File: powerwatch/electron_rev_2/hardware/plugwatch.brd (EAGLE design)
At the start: 57.1 x 93 mm, 87 parts, among them J1 TC2030-JLINK-NL, J2 DM3AT-SF-PEJM5, SW1 SIP3240X, SW2 SIP3240X, SW3 SIP3240X, SW4 SIP3240X, SW7 SIP3240X, U1 MAX-M8, U3 ISL29035, U37 MPU-9250, U4 NRF51822QF, U5 SAFFB1G56KB0F0A, U6 BGA725L6-ALT, U7 OPA322AIDBVT, U8 MAX740XESA, X3 16MHz, X4 ABS05-32.768KHZ-9-T

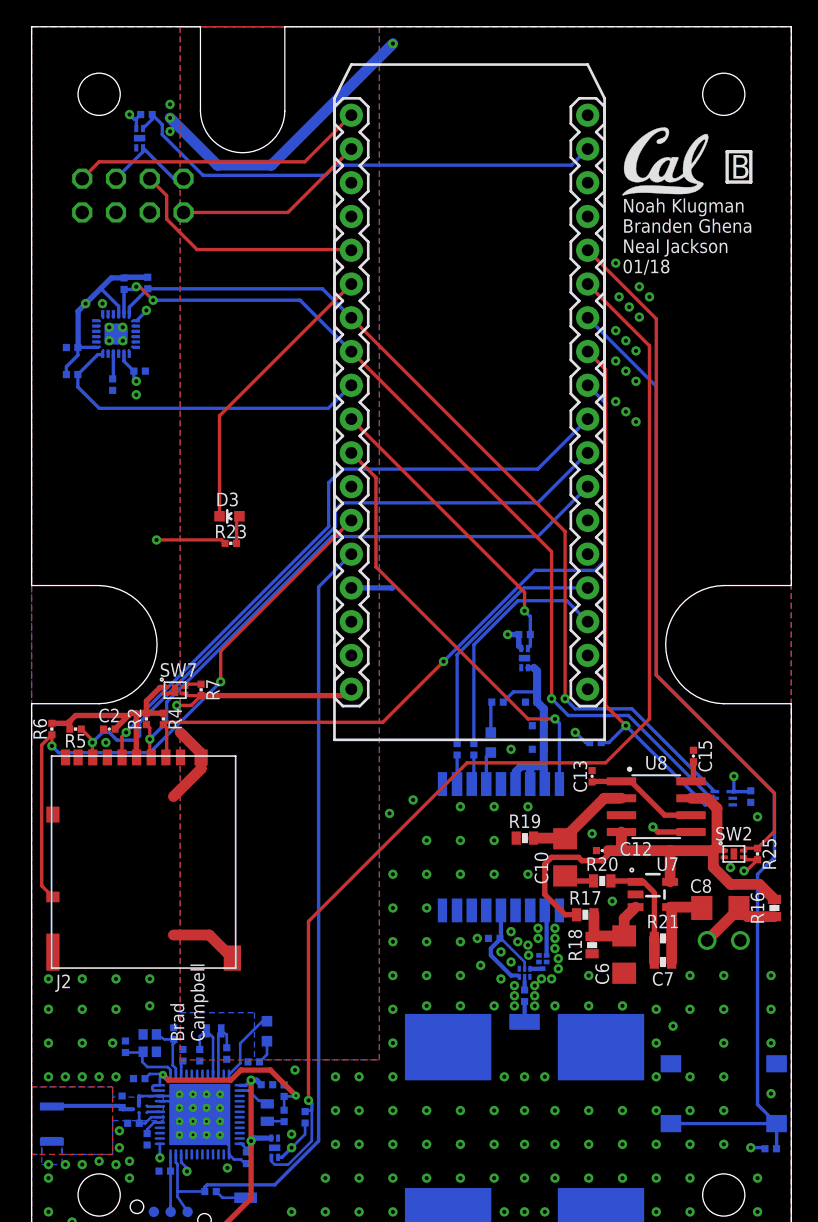
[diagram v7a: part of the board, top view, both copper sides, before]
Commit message: Add testpoints
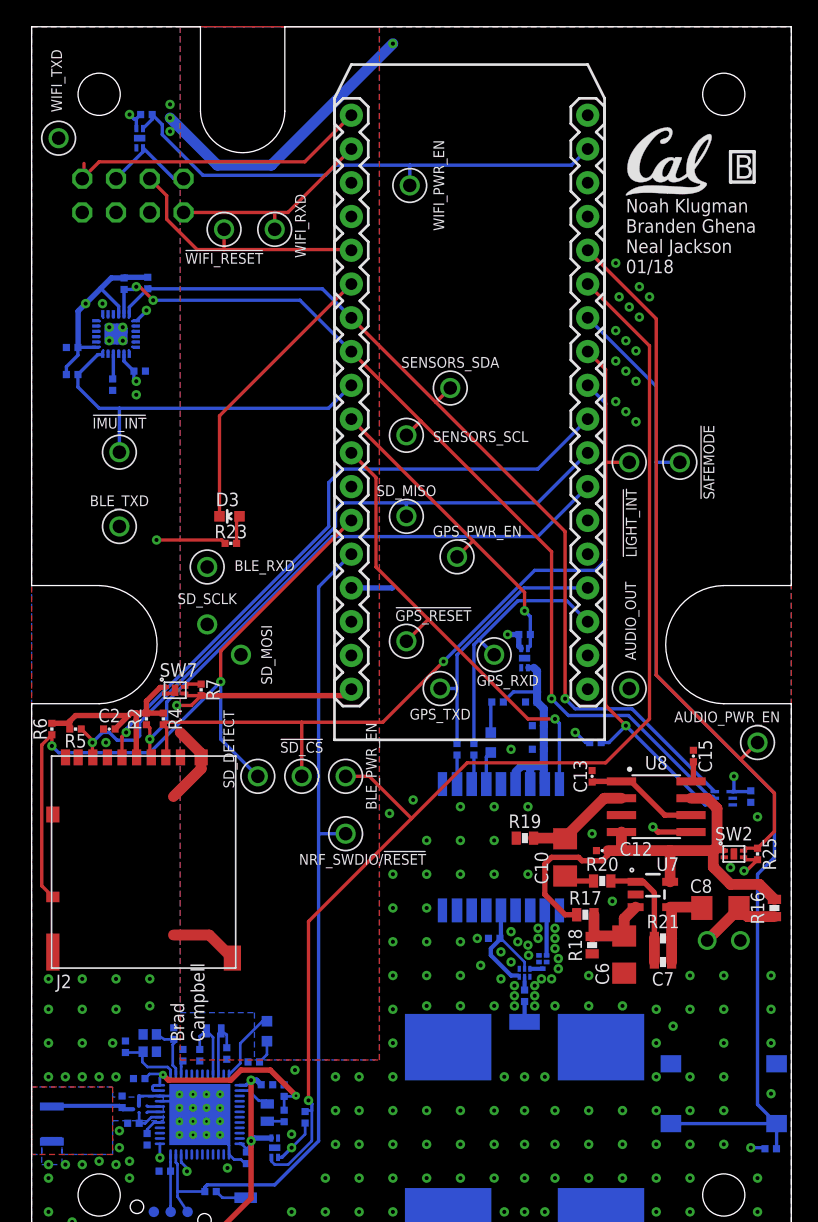
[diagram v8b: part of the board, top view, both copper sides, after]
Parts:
- added TP1, TP10, TP11, TP12, TP13, TP14, TP15, TP16, TP17, TP19, TP2, TP20, TP21, TP22, TP23, TP24, TP25, TP3, TP4, TP5, TP6, TP7, TP8, TP9: TEST_POINT_0.040IN, headers:TESTPOINT_0.040IN
- moved U$3 0.25 mm to (44.7, 80.3)
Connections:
- net !GPS_RESET: now also TP23.TESTPOINT
- net !IMU_INT: now also TP21.TESTPOINT
- net !LIGHT_INT: now also TP7.TESTPOINT
- net !SAFEMODE: now also TP8.TESTPOINT
- net !SD_CS: now also TP6.TESTPOINT
- net !SD_DETECT: now also TP24.TESTPOINT
- net !WIFI_RESET: now also TP17.TESTPOINT
- net AUDIO_OUT: now also TP11.TESTPOINT
- net AUDIO_PWR_EN: now also TP10.TESTPOINT
- net BLE_PWR_EN: now also TP9.TESTPOINT
- net BLE_RXD: now also TP16.TESTPOINT
- net BLE_TXD: now also TP15.TESTPOINT
- net GPS_PWR_EN: now also TP22.TESTPOINT
- net GPS_RXD: now also TP1.TESTPOINT
- net GPS_TXD: now also TP2.TESTPOINT
- net NRF_SWDIO/!RESET: now also TP25.TESTPOINT
- net SD_MISO: now also TP4.TESTPOINT
- net SD_MOSI: now also TP3.TESTPOINT
- net SD_SCLK: now also TP5.TESTPOINT
- net SENSORS_SCL: now also TP20.TESTPOINT
- net SENSORS_SDA: now also TP19.TESTPOINT
- net WIFI_PWR_EN: now also TP12.TESTPOINT
- net WIFI_RXD: now also TP14.TESTPOINT
- net WIFI_TXD: now also TP13.TESTPOINT
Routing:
- net !SD_DETECT: track 45.0 -> 53.3 mm
- net BLE_PWR_EN: track 87.9 -> 94.2 mm
- net !SD_CS: track 54.7 -> 58.8 mm
- net BLE_TXD: track 85.1 -> 88.6 mm
- net !IMU_INT: track 25.4 -> 28.7 mm
- net BLE_RXD: track 78.7 -> 81.2 mm
- net !GPS_RESET: track 32.6 -> 34.9 mm
- net NRF_SWDIO/!RESET: track 62.2 -> 64.2 mm
- net AUDIO_PWR_EN: track 52.5 -> 54.3 mm
- net !LIGHT_INT: track 40.9 -> 42.6 mm
- net !SAFEMODE: track 77.4 -> 79.2 mm
- net GPS_PWR_EN: track 22.9 -> 24.6 mm
- net GPS_RXD: track 18.0 -> 19.6 mm
- net SENSORS_SDA: track 68.3 -> 69.9 mm
- net SENSORS_SCL: track 68.7 -> 70.3 mm
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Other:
- board text added: "!GPS_RESET"
- board text added: "!IMU_INT"
- board text added: "!LIGHT_INT"
- board text added: "!SAFEMODE"
- board text added: "!SD_CS"
- board text added: "!WIFI_RESET"
- board text added: "AUDIO_OUT"
- board text added: "AUDIO_PWR_EN"
- board text added: "BLE_PWR_EN"
- board text added: "BLE_RXD"
- board text added: "BLE_TXD"
- board text added: "GPS_PWR_EN"
- board text added: "GPS_RXD"
- board text added: "GPS_TXD"
- board text added: "NRF_SWDIO/!RESET"
- board text added: "SD_DETECT"
- board text added: "SD_MISO"
- board text added: "SD_MOSI"
- board text added: "SD_SCLK"
- board text added: "SENSORS_SCL"
- board text added: "SENSORS_SDA"
- board text added: "WIFI_PWR_EN"
- board text added: "WIFI_RXD"
- board text added: "WIFI_TXD"
